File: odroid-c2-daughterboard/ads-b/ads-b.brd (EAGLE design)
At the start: 93.7 x 55.9 mm, 38 parts, among them U1 SEN-09403, U3 BMP180

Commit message: Updates from first schem review
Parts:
- added R17, R18, R19: 0, rcl:R0603
- R12, R301, R302: value 10K -> 1K
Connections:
- new net N$11: R17.2, U4.9
- new net N$12: R18.2, U4.11
- new net N$13: R19.2, U4.1
- net CO2_AD: now also JP3.P40
- net GND: now also R17.1, R18.1, R19.1
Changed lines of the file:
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@@
 <element name="LED301" library="led" package="SML0603" value="" x="3.81" y="22.86"/>
 <element name="LED302" library="led" package="SML0603" value="" x="3.81" y="33.02"/>
-<element name="R301" library="rcl" package="R0603" value="10K" x="7.62" y="22.86"/>
-<element name="R302" library="rcl" package="R0603" value="10K" x="7.62" y="33.02"/>
+<element name="R301" library="rcl" package="R0603" value="1K" x="7.62" y="22.86"/>
+<element name="R302" library="rcl" package="R0603" value="1K" x="7.62" y="33.02"/>
 <element name="JP3" library="connectors" package="2X20" value="" x="-31.623" y="-108.585"/>
 <element name="U$2" library="ubloxLib" package="UBLOX_CAM" value="UBLOX_CAM" x="-73.152" y="-132.207"/>
@@
 <element name="Q2" library="transistor-power" package="SO-08" value="" x="-92.202" y="-205.74"/>
 <element name="R11" library="rcl" package="R0603" value="220" x="-94.869" y="-212.217"/>
-<element name="R12" library="rcl" package="R0603" value="10K" x="-94.869" y="-217.17"/>
+<element name="R12" library="rcl" package="R0603" value="1K" x="-94.869" y="-217.17"/>
 <element name="LED1" library="led" package="SML0603" value="" x="-94.869" y="-222.504"/>
 <element name="R13" library="rcl" package="R0603" value="4.7k" x="-94.869" y="-225.933"/>
@@
 <element name="R5" library="rcl" package="R0603" value="10K" x="-94.869" y="-272.796"/>
 <element name="R6" library="rcl" package="R0603" value="10K" x="-94.869" y="-277.749"/>
+<element name="R17" library="rcl" package="R0603" value="0" x="-94.869" y="-282.702"/>
+<element name="R18" library="rcl" package="R0603" value="0" x="-94.869" y="-287.655"/>
+<element name="R19" library="rcl" package="R0603" value="0" x="-94.869" y="-292.608"/>
 </elements>
 <signals>
@@
 <contactref element="C7" pad="2"/>
 <contactref element="R6" pad="1"/>
+<contactref element="R17" pad="1"/>
+<contactref element="R18" pad="1"/>
+<contactref element="R19" pad="1"/>
 <wire x1="-79.16" y1="-177.546" x2="-79.16" y2="-172.593" width="0" layer="19" extent="1-1"/>
 <wire x1="-85.256" y1="-177.546" x2="-79.16" y2="-177.546" width="0" layer="19" extent="1-1"/>
@@
 <wire x1="-94.019" y1="-267.843" x2="-94.019" y2="-257.937" width="0" layer="19" extent="1-1"/>
 <wire x1="-95.719" y1="-277.749" x2="-94.019" y2="-267.843" width="0" layer="19" extent="1-1"/>
+<wire x1="-95.719" y1="-282.702" x2="-95.719" y2="-277.749" width="0" layer="19" extent="1-1"/>
+<wire x1="-95.719" y1="-287.655" x2="-95.719" y2="-282.702" width="0" layer="19" extent="1-1"/>
+<wire x1="-95.719" y1="-292.608" x2="-95.719" y2="-287.655" width="0" layer="19" extent="1-1"/>
 <wire x1="3.06" y1="22.86" x2="-17.653" y2="-107.315" width="0" layer="19" extent="1-1"/>
 <wire x1="3.06" y1="33.02" x2="3.06" y2="22.86" width="0" layer="19" extent="1-1"/>
@@
 <contactref element="R16" pad="1"/>
 <contactref element="C6" pad="1"/>
-<wire x1="-95.719" y1="-257.937" x2="-95.719" y2="-262.89" width="0" layer="19" extent="1-1"/>
+<contactref element="JP3" pad="P40"/>
+<wire x1="-95.719" y1="-257.937" x2="-55.753" y2="-109.855" width="0" layer="19" extent="1-1"/>
+<wire x1="-95.719" y1="-262.89" x2="-95.719" y2="-257.937" width="0" layer="19" extent="1-1"/>
 </signal>
 <signal name="N$10">
@@
 <wire x1="-94.019" y1="-277.749" x2="-95.719" y2="-272.796" width="0" layer="19" extent="1-1"/>
 </signal>
+<signal name="N$11">
+<contactref element="U4" pad="9"/>
+<contactref element="R17" pad="2"/>
+<wire x1="-94.019" y1="-282.702" x2="-76.831" y2="-168.878" width="0" layer="19" extent="1-1"/>
+</signal>
+<signal name="N$12">
+<contactref element="U4" pad="11"/>
+<contactref element="R18" pad="2"/>
+<wire x1="-94.019" y1="-287.655" x2="-75.831" y2="-168.878" width="0" layer="19" extent="1-1"/>
+</signal>
+<signal name="N$13">
+<contactref element="U4" pad="1"/>
+<contactref element="R19" pad="2"/>
+<wire x1="-94.019" y1="-292.608" x2="-78.581" y2="-165.628" width="0" layer="19" extent="1-1"/>
+</signal>
 </signals>

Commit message: basic floorplanning. redefined the origin-area as the shape ryan drew elsewhere. moved all the stuffs into the new board. laid out components to be in logical groups. to-do: begin defining power/ground routing. chooch.
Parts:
- moved R19 363.8 mm to (78.1, 27.4)
- moved R17 357.4 mm to (78.1, 30.1)
- moved R18 357.1 mm to (78.1, 24.8)
- moved LED1 319.8 mm to (82.7, 43.4), turned to 180 degrees
- moved R12 313.2 mm to (78.9, 43.4), turned to 180 degrees
- moved R6 311.7 mm to (11.4, 15.2), turned to 90 degrees
- moved C7 311.6 mm to (9.14, 25.9)
- moved R5 308.1 mm to (14.5, 15.2), turned to 90 degrees
- moved R16 306.2 mm to (14.1, 23.2)
- moved C6 304.9 mm to (18.3, 25.1), turned to 90 degrees
- moved R15 299.4 mm to (14.1, 25.9)
- moved U1 298.6 mm to (14.5, 38.5)
- moved R14 288.9 mm to (29.0, 30.1), turned to 90 degrees
- moved R13 266.1 mm to (17.5, 15.2), turned to 90 degrees
- moved R9 262.0 mm to (80.8, 14.5), turned to 270 degrees
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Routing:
- removed copper zone on layer 1, net N$16
- removed copper zone on layer 16, net N$17
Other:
- board size 93.7 x 55.9 mm -> 85.7 x 56 mm

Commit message: agile as a motherfucker. added a few 5V power traces. connected a few things to a few other things. incremental.
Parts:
- moved JP5 9.18 mm to (11.8, 14.1)
- moved JP4 5.42 mm to (6.10, 13.7)
- moved R6 3.14 mm to (12.2, 18.3)
- moved R5 3.07 mm to (14.9, 18.3), turned to 270 degrees
- moved R10 3.05 mm to (20.6, 18.3)
- moved R11 3.05 mm to (8.38, 18.3)
- moved R13 3.05 mm to (17.5, 18.3)
- moved Q2 1.20 mm to (16.4, 4.95)
- moved S2 1.20 mm to (6.10, 4.19)
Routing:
- net +5V: track 0.00 -> 91.0 mm
- net N$10: track 0.00 -> 19.8 mm
- net N$7: track 0.00 -> 12.5 mm
- net SWITCH_MONITOR: track 0.00 -> 2.67 mm

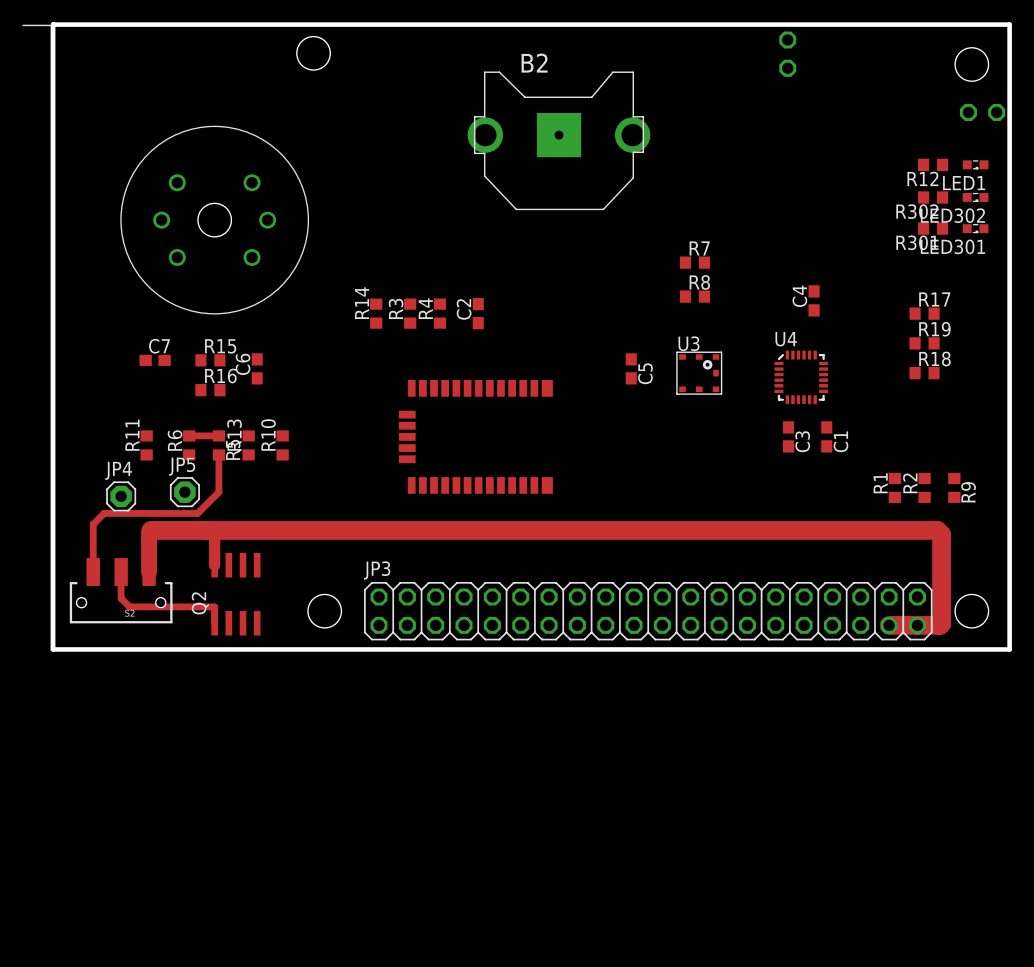
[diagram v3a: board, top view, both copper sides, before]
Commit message: Fix ODROID-C2 board outline, add pull-ups for FETs
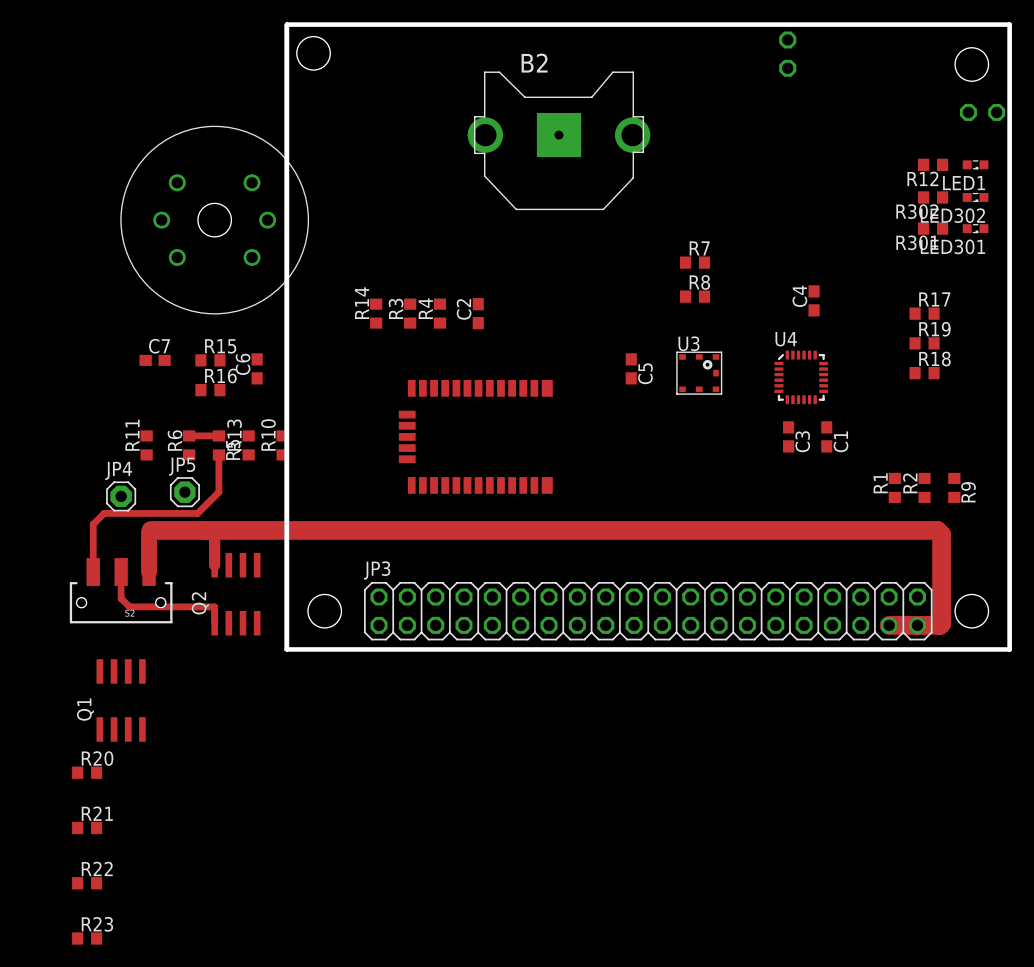
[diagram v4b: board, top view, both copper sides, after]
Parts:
- added Q1: (no value), transistor-power:SO-08
- added R20: 220, rcl:R0603
- added R21: 1k, rcl:R0603
- added R22, R23: 10K, rcl:R0603
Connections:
- new net HEATER_ENABLE: R20.2, R21.2
- new net N$14: Q1.5, Q1.6, Q1.7, Q1.8, U1.HA
- new net N$16: Q1.4, R20.1
- net +3V3: now also R21.1
- net +5V: now also Q1.1, Q1.2, Q1.3; no longer U1.HA, U1.HB
- net GND: now also R23.1, U1.HB
- net N$7: now also R22.2
- net N$9: now also R22.1, R23.2
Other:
- board size 85.7 x 56 mm -> 64.8 x 56 mm
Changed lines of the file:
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@@
 <board>
 <plain>
-<wire x1="0" y1="56.007" x2="0" y2="0" width="0.4064" layer="20"/>
-<wire x1="0" y1="0" x2="85.725" y2="0" width="0.4064" layer="20"/>
+<wire x1="20.955" y1="56.007" x2="20.955" y2="0" width="0.4064" layer="20"/>
+<wire x1="20.955" y1="0" x2="85.725" y2="0" width="0.4064" layer="20"/>
 <wire x1="85.725" y1="0" x2="85.725" y2="56.007" width="0.4064" layer="20"/>
-<wire x1="85.725" y1="56.007" x2="0" y2="56.007" width="0.4064" layer="20"/>
+<wire x1="85.725" y1="56.007" x2="20.955" y2="56.007" width="0.4064" layer="20"/>
 </plain>
 <attributes>
@@
 <element name="R18" library="rcl" package="R0603" value="0" x="78.105" y="24.765"/>
 <element name="R19" library="rcl" package="R0603" value="0" x="78.105" y="27.432"/>
+<element name="Q1" library="transistor-power" package="SO-08" value="" x="6.096" y="-4.572"/>
+<element name="R20" library="rcl" package="R0603" value="220" x="3.048" y="-11.049"/>
+<element name="R21" library="rcl" package="R0603" value="1k" x="3.048" y="-16.002"/>
+<element name="R22" library="rcl" package="R0603" value="10K" x="3.048" y="-20.955"/>
+<element name="R23" library="rcl" package="R0603" value="10K" x="3.048" y="-25.908"/>
 </elements>
 <signals>
@@
 <contactref element="R18" pad="1"/>
 <contactref element="R19" pad="1"/>
+<contactref element="U1" pad="HB"/>
+<contactref element="R23" pad="1"/>
 <wire x1="83.427" y1="40.513" x2="83.427" y2="43.434" width="0" layer="19" extent="1-1"/>
 <wire x1="83.427" y1="37.719" x2="83.427" y2="40.513" width="0" layer="19" extent="1-1"/>
@@
 <wire x1="9.994" y1="25.908" x2="13.247" y2="25.908" width="0" layer="19" extent="1-1"/>
 <wire x1="18.288" y1="25.996" x2="13.247" y2="25.908" width="0" layer="19" extent="1-1"/>
+<wire x1="19.228" y1="38.481" x2="18.288" y2="25.996" width="0" layer="19" extent="1-1"/>
 <wire x1="45.339" y1="46.101" x2="38.1" y2="30.949" width="0" layer="19" extent="1-1"/>
+<wire x1="2.198" y1="-25.908" x2="29.21" y2="4.699" width="0" layer="19" extent="1-1"/>
 </signal>
 <signal name="GPS_RXD">
@@
 <contactref element="U1" pad="A1"/>
 <contactref element="C7" pad="1"/>
+<contactref element="R21" pad="1"/>
 <wire x1="69.056" y1="23.134" x2="78.017" y2="37.719" width="0" layer="19" extent="1-1"/>
 <wire x1="66.306" y1="22.384" x2="69.056" y2="23.134" width="0" layer="19" extent="1-1"/>
@@
 <wire x1="8.294" y1="25.908" x2="20.574" y2="19.138" width="0" layer="19" extent="1-1"/>
 <wire x1="11.128" y1="41.831" x2="8.294" y2="25.908" width="0" layer="19" extent="1-1"/>
+<wire x1="2.198" y1="-16.002" x2="20.574" y2="19.138" width="0" layer="19" extent="1-1"/>
 </signal>
 <signal name="+5V">
@@
 <contactref element="Q2" pad="5"/>
 <contactref element="Q2" pad="8"/>
-<contactref element="U1" pad="HB"/>
-<contactref element="U1" pad="HA"/>
 <wire x1="77.47" y1="2.159" x2="79.502" y2="2.159" width="1.6764" layer="1"/>
 <wire x1="79.502" y1="2.159" x2="79.629" y2="2.286" width="1.6764" layer="1"/>
@@
 <wire x1="14.478" y1="7.553" x2="14.478" y2="9.906" width="1.016" layer="1"/>
 <wire x1="14.478" y1="9.906" x2="13.716" y2="10.668" width="0.6096" layer="1"/>
-<wire x1="9.728" y1="38.481" x2="19.228" y2="38.481" width="0" layer="19" extent="1-1"/>
-<wire x1="8.763" y1="10.668" x2="9.728" y2="38.481" width="0" layer="19" extent="1-1"/>
-<wire x1="15.748" y1="7.553" x2="14.478" y2="7.553" width="0" layer="19" extent="1-1"/>
-<wire x1="17.018" y1="7.553" x2="15.748" y2="7.553" width="0" layer="19" extent="1-1"/>
-<wire x1="18.288" y1="7.553" x2="17.018" y2="7.553" width="0" layer="19" extent="1-1"/>
+<contactref element="Q1" pad="1"/>
+<contactref element="Q1" pad="2"/>
+<contactref element="Q1" pad="3"/>
+<wire x1="17.018" y1="7.553" x2="18.288" y2="7.553" width="0" layer="19" extent="1-1"/>
+<wire x1="15.748" y1="7.553" x2="17.018" y2="7.553" width="0" layer="19" extent="1-1"/>
+<wire x1="14.478" y1="7.553" x2="15.748" y2="7.553" width="0" layer="19" extent="1-1"/>
+<wire x1="6.731" y1="-7.172" x2="8.596" y2="6.941" width="0" layer="19" extent="1-1"/>
+<wire x1="5.461" y1="-7.172" x2="6.731" y2="-7.172" width="0" layer="19" extent="1-1"/>
+<wire x1="4.191" y1="-7.172" x2="5.461" y2="-7.172" width="0" layer="19" extent="1-1"/>
 </signal>
 <signal name="USER_LED0">
@@
 <wire x1="6.858" y1="3.81" x2="14.478" y2="3.81" width="0.6096" layer="1"/>
 <wire x1="14.478" y1="3.81" x2="14.478" y2="2.353" width="0.6096" layer="1"/>
+<contactref element="R22" pad="2"/>
 <wire x1="6.096" y1="6.941" x2="6.096" y2="13.716" width="0" layer="19" extent="1-1"/>
 <wire x1="15.748" y1="2.353" x2="14.478" y2="2.353" width="0" layer="19" extent="1-1"/>
 <wire x1="17.018" y1="2.353" x2="15.748" y2="2.353" width="0" layer="19" extent="1-1"/>
+<wire x1="3.898" y1="-20.955" x2="6.858" y2="3.81" width="0" layer="19" extent="1-1"/>
 </signal>
 <signal name="N$9">
 <contactref element="Q2" pad="4"/>
 <contactref element="R11" pad="1"/>
+<contactref element="R23" pad="2"/>
+<contactref element="R22" pad="1"/>
 <wire x1="18.288" y1="2.353" x2="8.382" y2="17.438" width="0" layer="19" extent="1-1"/>
+<wire x1="2.198" y1="-20.955" x2="18.288" y2="2.353" width="0" layer="19" extent="1-1"/>
+<wire x1="3.898" y1="-25.908" x2="2.198" y2="-20.955" width="0" layer="19" extent="1-1"/>
 </signal>
 <signal name="KEEP_ALIVE">
@@
 <wire x1="65.056" y1="25.634" x2="78.955" y2="27.432" width="0" layer="19" extent="1-1"/>
 </signal>
+<signal name="N$14">
+<contactref element="U1" pad="HA"/>
+<contactref element="Q1" pad="5"/>
+<contactref element="Q1" pad="8"/>
+<contactref element="Q1" pad="7"/>
+<contactref element="Q1" pad="6"/>
+<wire x1="8.001" y1="-1.972" x2="9.728" y2="38.481" width="0" layer="19" extent="1-1"/>
+<wire x1="6.731" y1="-1.972" x2="8.001" y2="-1.972" width="0" layer="19" extent="1-1"/>
+<wire x1="5.461" y1="-1.972" x2="6.731" y2="-1.972" width="0" layer="19" extent="1-1"/>
+<wire x1="4.191" y1="-1.972" x2="5.461" y2="-1.972" width="0" layer="19" extent="1-1"/>
+</signal>
+<signal name="HEATER_ENABLE">
+<contactref element="R20" pad="2"/>
+<contactref element="R21" pad="2"/>
+<wire x1="3.898" y1="-11.049" x2="3.898" y2="-16.002" width="0" layer="19" extent="1-1"/>
+</signal>
+<signal name="N$16">
+<contactref element="R20" pad="1"/>
+<contactref element="Q1" pad="4"/>
+<wire x1="8.001" y1="-7.172" x2="2.198" y2="-11.049" width="0" layer="19" extent="1-1"/>
+</signal>
 </signals>
